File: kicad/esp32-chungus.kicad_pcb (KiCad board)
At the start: 2 copper layers, 26.5 x 38.8 mm, 20 parts, among them J1 47346-1001, J2 Conn_01x11, J3 Conn_01x11, U1 ESP32-S3-WROOM-1, U2 REG1117-3.3, U3 WS2812B

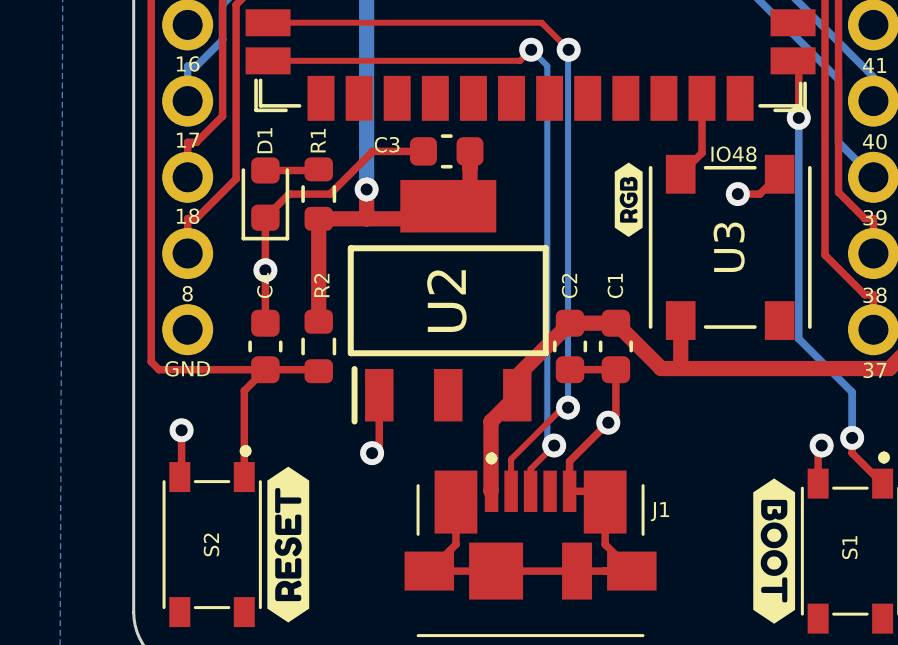
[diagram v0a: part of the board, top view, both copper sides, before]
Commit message: switch to low quiescent current voltage regulator, add BOM to README.md
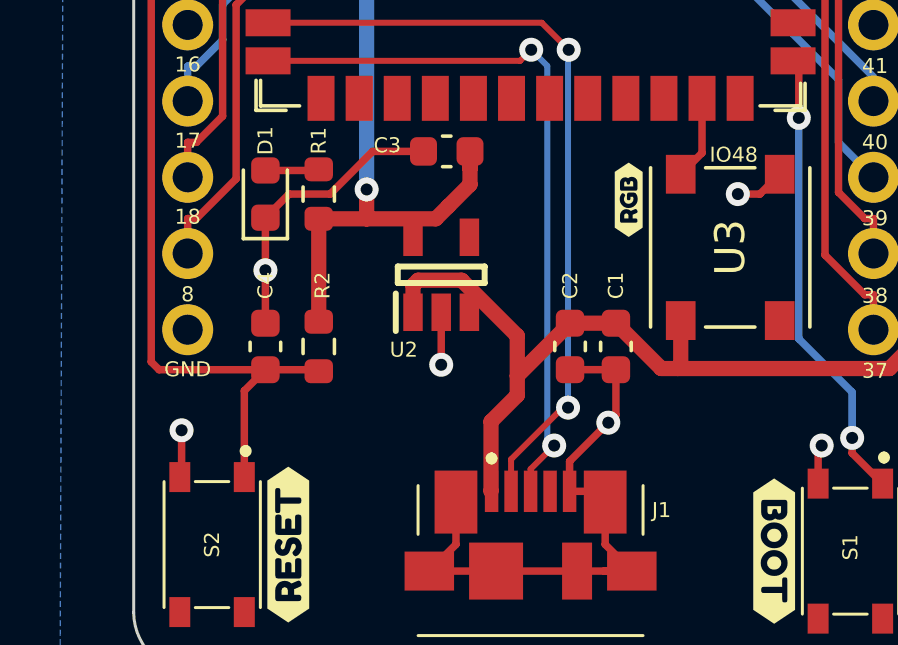
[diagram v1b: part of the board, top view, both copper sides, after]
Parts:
- removed REF**: OSHW-Symbol_8.9x8mm_SilkScreen, Symbol:OSHW-Symbol_8.9x8mm_SilkScreen
- U2: value REG1117-3.3 -> RT9080-33GJ5; footprint SamacSys_Parts:SOT230P700X180-4N -> SamacSys_Parts:SOT94P280X100-5N
- moved U2 0.90 mm to (141.8, 101.8)
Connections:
- U1 pad 15: /GPIO3 -> unconnected-(U1-Pad15)
- U1 pad 16: /GPIO46 -> unconnected-(U1-Pad16)
- U1 pad 18: /GPIO10 -> unconnected-(U1-Pad18)
- U1 pad 19: /GPIO11 -> unconnected-(U1-Pad19)
- U1 pad 20: /GPIO12 -> unconnected-(U1-Pad20)
- U1 pad 21: /GPIO13 -> unconnected-(U1-Pad21)
- U1 pad 22: /GPIO14 -> unconnected-(U1-Pad22)
- U1 pad 23: /GPIO21 -> unconnected-(U1-Pad23)
- U1 pad 24: /GPIO47 -> unconnected-(U1-Pad24)
- U1 pad 26: /GPIO45 -> unconnected-(U1-Pad26)
- U1 pad 28: /GPIO35 -> unconnected-(U1-Pad28)
- U1 pad 29: /GPIO36 -> unconnected-(U1-Pad29)
- U2 pad 1: GND -> +5V
- U2 pad 2: unconnected-(U2-Pad2) -> GND
- U2 pad 4: +3.3V -> (no net)
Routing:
- net +5V: track 48.1 -> 54.7 mm

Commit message: clean up board and schematic
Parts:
- moved J1 0.63 mm to (144.7, 111.5)
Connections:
- U2 pad 4: (no net) -> unconnected-(U2-Pad4)
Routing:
- net GND: track 43.5 -> 41.8 mm
- net +5V: track 54.7 -> 55.3 mm
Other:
- board text added: "ESP Chungus r3 by ayan4m1"
- board text removed: "ESP Chungus r2 by ayan4m1"
